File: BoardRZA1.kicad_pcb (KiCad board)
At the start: 4 copper layers, 99.9 x 80 mm, 151 parts, among them CON1 USB-MINI-B, CON2 USB-MINI-B, CON3 con-microSD, CON4 BARREL_JACK, J1 HR911105A, J2 SIL38, P1 CONN_5X2, SW1 RESET, SW2 NMI, SW3 SW0, SW4 SW1, U1 RZ-A1L, U2 OSC_4PIN, U3 OSC_4PIN, U4 N25QXXX, U5 AS4C16M16S, U6 BA3259HFP, U7 BU42xx, U8 KSZ8041MLL, U9 25MHz, X1 32.768k

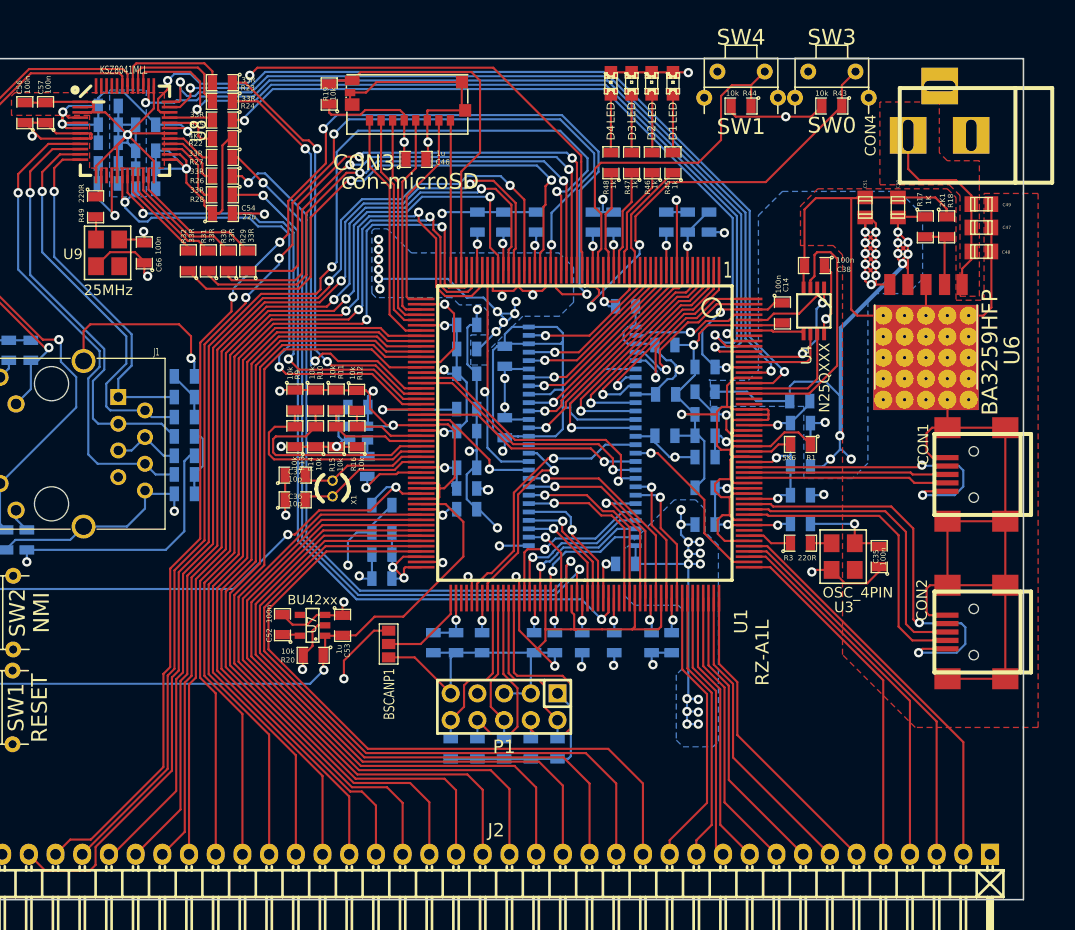
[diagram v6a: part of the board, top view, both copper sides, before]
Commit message: USB-B CON2 -> USB-A CON2
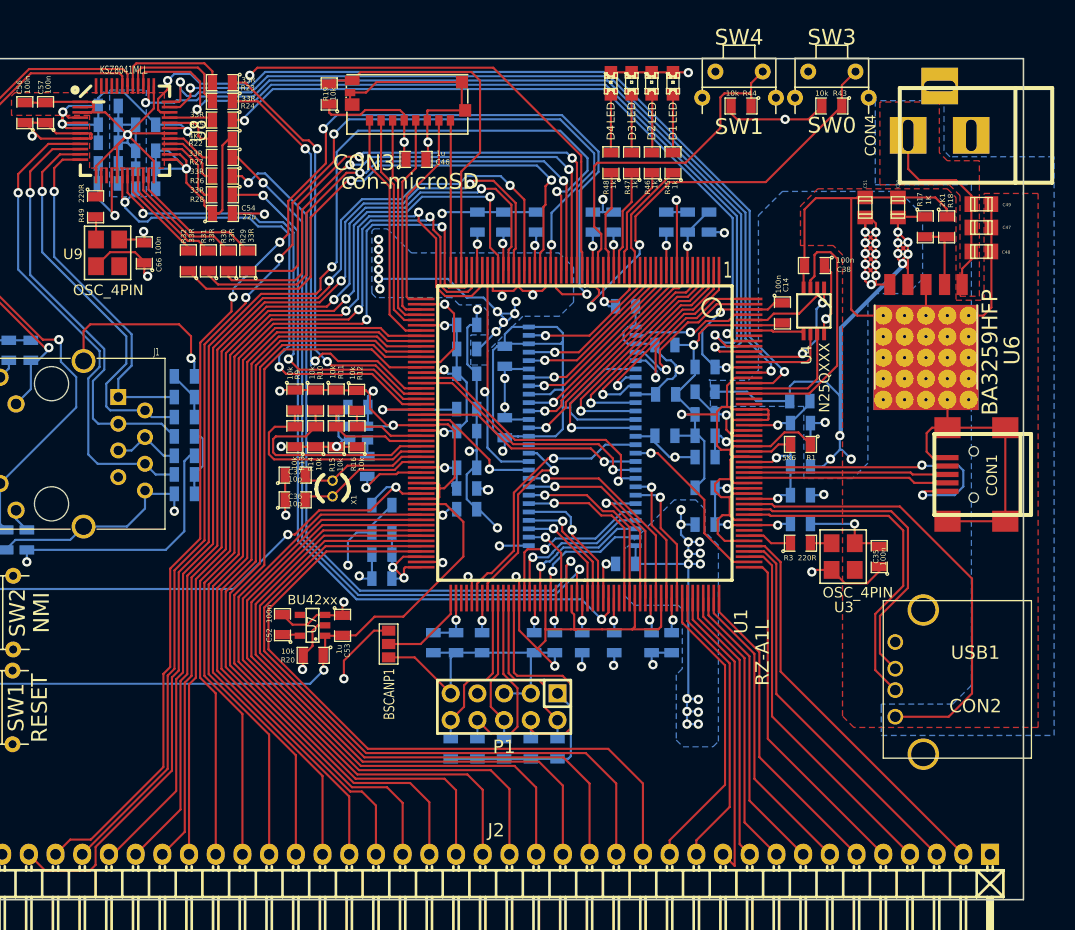
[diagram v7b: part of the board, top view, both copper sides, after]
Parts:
- CON2: value USB-MINI-B -> USB1; footprint Connect:USB_MINI_B -> Connect:USB_A
- U9: value 25MHz -> OSC_4PIN
- moved CON2 9.46 mm to (107.6, 76.6), turned to 0 degrees
- moved SW4 0.19 mm to (92.8, 20.1)
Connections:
- C47 pad 1: Net-(C47-Pad1) -> /+5v
- C48 pad 1: Net-(C47-Pad1) -> /+5v
- C49 pad 1: Net-(C47-Pad1) -> /+5v
- CON2 pad 1: Net-(CON2-Pad1) -> /+5v
- CON2 pad 4: Net-(CON2-Pad4) -> VSS
- CON2 pad 5: VSS -> (no net)
- CON2 pad 6: VSS -> (no net)
- CON4 pad 1: Net-(C47-Pad1) -> /+5v
- U1 pad 169: Net-(CON2-Pad1) -> /+5v
- U6 pad 1: Net-(C47-Pad1) -> /+5v
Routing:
- net /+5v: track 0.00 -> 62.4 mm
- net Net-(CON2-Pad1): track 39.7 -> 0.00 mm, vias 2 -> 0
- net VSS: track 629.8 -> 591.3 mm
- net Net-(C47-Pad1): track 19.1 -> 0.00 mm
- net Net-(CON2-Pad2): track 28.8 -> 32.4 mm
- net /P1_2: track 25.6 -> 28.7 mm
- net Net-(CON2-Pad3): track 28.7 -> 31.0 mm
- net /P1_0: track 26.8 -> 28.2 mm
- net /P1_1: track 25.9 -> 27.4 mm
- net +3.3V: track 313.9 -> 314.8 mm
- added copper zone on B.Cu, net /+5v

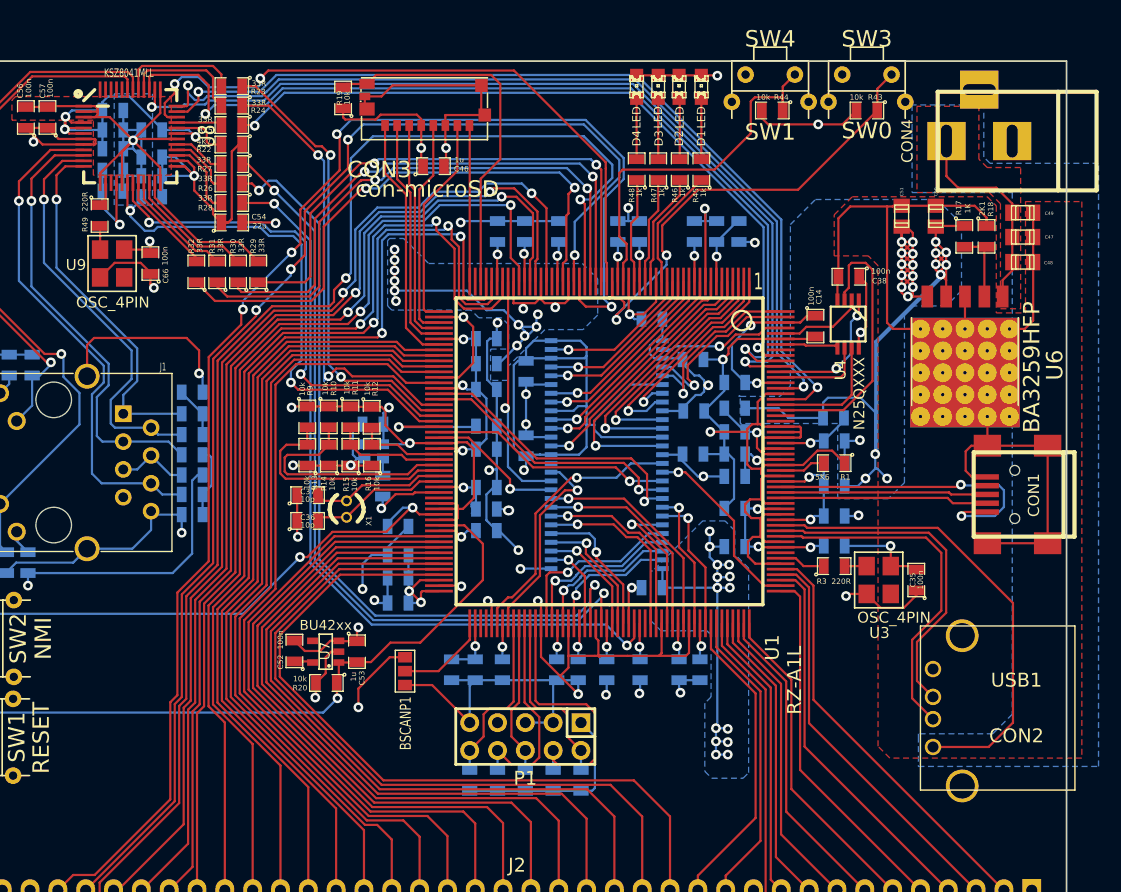
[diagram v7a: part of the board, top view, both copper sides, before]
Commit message: Add power from mini usb-b Prettify 3D
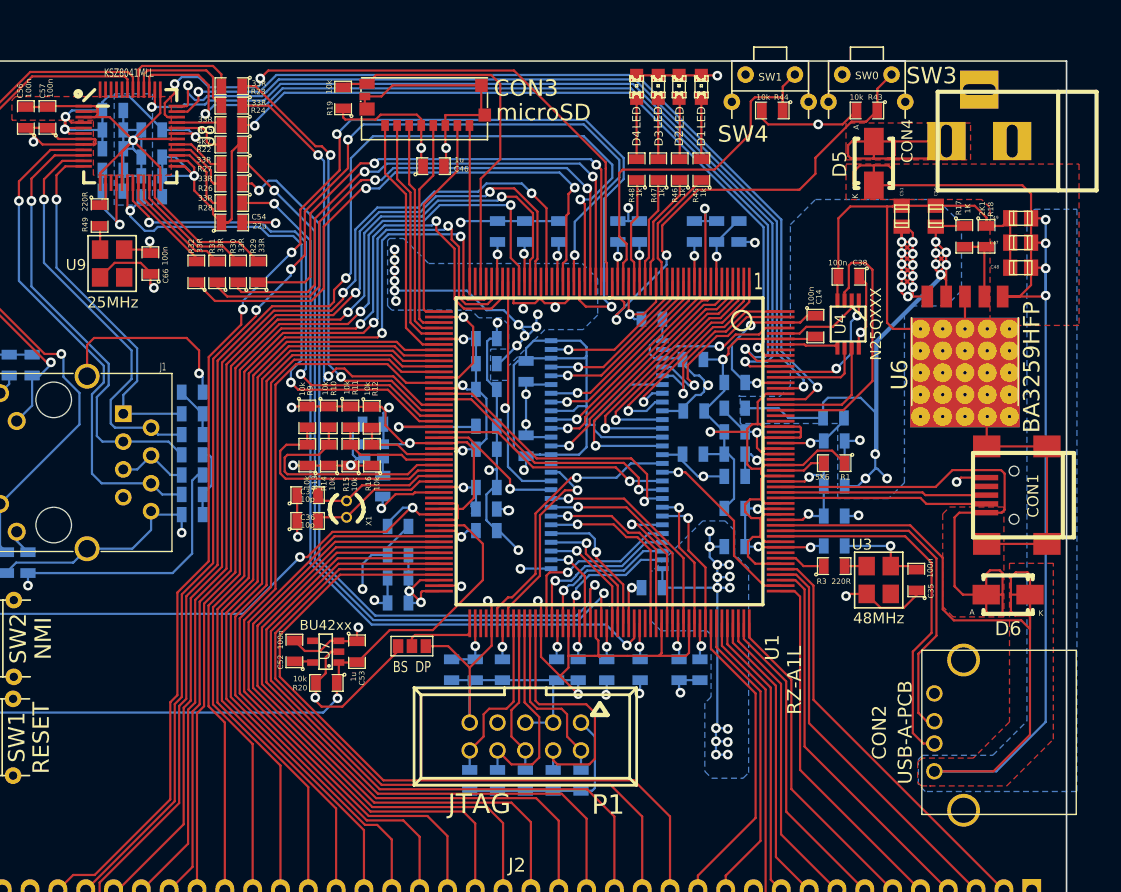
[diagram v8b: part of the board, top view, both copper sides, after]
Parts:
- added D5: MBRA210, Diodes_SMD:Diode-SMA_Standard, F.Cu at (102.2, 26.9)
- added D6: MBRA210, Diodes_SMD:Diode-SMA_Standard, F.Cu at (114.5, 66.3)
- BS  DP: renamed from BSCANP1
- CON2: value USB1 -> USB-A-PCB
- CON3: value con-microSD -> microSD
- P1: value CONN_5X2 -> JTAG; footprint Pin_Headers:Pin_Header_Straight_2x05 -> Connect:VASCH5x2
- U2: value OSC_4PIN -> 13MHz
- U3: value OSC_4PIN -> 48MHz
- U9: value OSC_4PIN -> 25MHz
- moved BS  DP 2.37 mm to (60.1, 71.0), turned to 90 degrees
- moved CON2 2.23 mm to (107.8, 78.9)
- moved C49 0.54 mm to (115.6, 31.9), turned to 0 degrees
- moved C47 0.54 mm to (115.6, 34.2), turned to 0 degrees
- moved C48 0.54 mm to (115.6, 36.4), turned to 0 degrees
- moved CON1 0.09 mm to (115.9, 57.2)
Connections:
- CON4 pad 1: /+5v -> Net-(CON4-Pad1)
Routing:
- net /+5v: track 62.4 -> 169.0 mm, vias 0 -> 4
- net Net-(CON4-Pad1): track 0.00 -> 23.5 mm
- net Net-(CON1-Pad1): track 28.9 -> 51.0 mm, vias 2 -> 0
- net +3.3V: track 314.8 -> 317.7 mm, vias 55 -> 54
- net Net-(BSCANP1-Pad2): track 8.60 -> 7.08 mm
- net VSS: track 591.3 -> 590.2 mm, vias 37 -> 38
- net Net-(CON2-Pad2): track 32.4 -> 33.4 mm
- net Net-(CON2-Pad3): track 31.0 -> 31.8 mm
- net /SW0: track 43.0 -> 43.9 mm
- added copper zone on F.Cu, net /+5v
- added copper zone on F.Cu, net Net-(CON1-Pad1)
- added copper zone on F.Cu, net Net-(CON4-Pad1)
- removed copper zone on F.Cu, net Net-(C47-Pad1)
